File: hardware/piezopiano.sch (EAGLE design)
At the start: 87 parts, among them J1 CON2, Q1 DMN3404L, Q2 DMN3404L, Q3 DMN3404L, Q4 DMN3404L, Q5 DMN3404L, Q6 DMN3404L, Q7 DMN3404L, Q8 DMN3404L, U1 ATMEGA4809, U2 CH340E_MSOP10

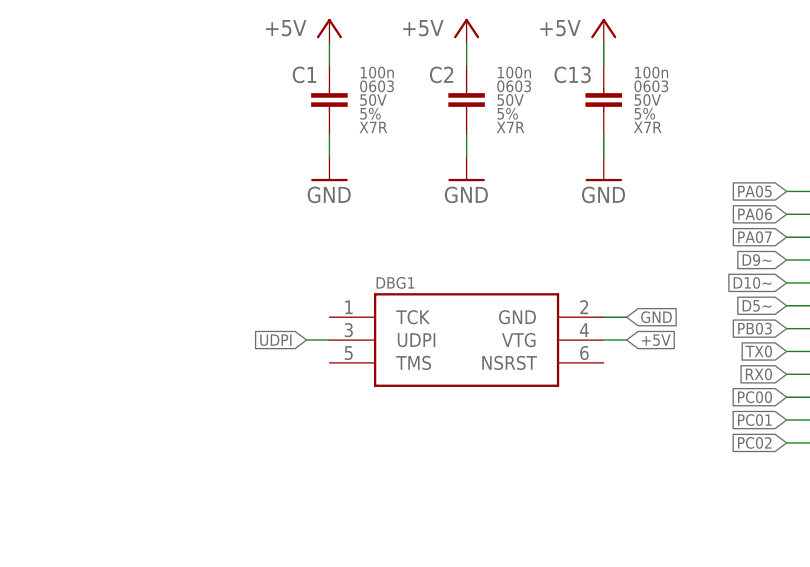
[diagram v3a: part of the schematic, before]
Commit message: Added PCB artwork
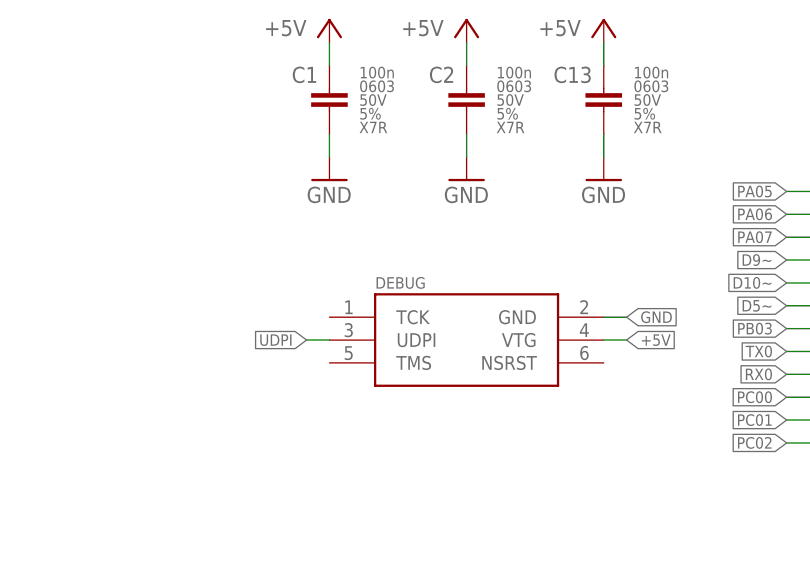
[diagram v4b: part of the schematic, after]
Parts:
- renumbered DBG1 to DEBUG
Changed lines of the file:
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@@
 <part name="R22" library="zaan-Resistors" library_urn="urn:adsk.eagle:library:16759442" deviceset="1KOHM" device="-0603-1/10W-1%" package3d_urn="urn:adsk.eagle:package:16759452/3" value="1k"/>
 <part name="U1" library="zaan-IC-Microcontroller" library_urn="urn:adsk.eagle:library:16759236" deviceset="ATMEGA4809" device="" package3d_urn="urn:adsk.eagle:package:30825331/1" value="ATMEGA4809"/>
-<part name="DBG1" library="zaan-Connectors" library_urn="urn:adsk.eagle:library:16759010" deviceset="AVR-UPDI-6" device="-SKEDD" package3d_urn="urn:adsk.eagle:package:16760574/1"/>
+<part name="DEBUG" library="zaan-Connectors" library_urn="urn:adsk.eagle:library:16759010" deviceset="AVR-UPDI-6" device="-SKEDD" package3d_urn="urn:adsk.eagle:package:16760574/1"/>
 <part name="C13" library="zaan-Capacitors" library_urn="urn:adsk.eagle:library:16758934" deviceset="100NF" device="-0603-50V-5%" package3d_urn="urn:adsk.eagle:package:16758953/4" value="100n"/>
 <part name="GND42" library="supply1" library_urn="urn:adsk.eagle:library:371" deviceset="GND" device=""/>
@@
 <part name="C11" library="zaan-Capacitors" library_urn="urn:adsk.eagle:library:16758934" deviceset="100NF" device="-0603-50V-5%" package3d_urn="urn:adsk.eagle:package:16758953/4" value="100n"/>
 <part name="GND37" library="supply1" library_urn="urn:adsk.eagle:library:371" deviceset="GND" device=""/>
-<part name="JP1" library="zaan-No-Category" library_urn="urn:adsk.eagle:library:16759360" deviceset="PINROW-1X5" device="" package3d_urn="urn:adsk.eagle:package:31104797/4"/>
-<part name="JP2" library="zaan-No-Category" library_urn="urn:adsk.eagle:library:16759360" deviceset="PINROW-1X5" device="" package3d_urn="urn:adsk.eagle:package:31104797/4"/>
-<part name="JP3" library="zaan-No-Category" library_urn="urn:adsk.eagle:library:16759360" deviceset="PINROW-1X5" device="" package3d_urn="urn:adsk.eagle:package:31104797/4"/>
-<part name="JP4" library="zaan-No-Category" library_urn="urn:adsk.eagle:library:16759360" deviceset="PINROW-1X5" device="" package3d_urn="urn:adsk.eagle:package:31104797/4"/>
-<part name="JP5" library="zaan-No-Category" library_urn="urn:adsk.eagle:library:16759360" deviceset="PINROW-1X5" device="" package3d_urn="urn:adsk.eagle:package:31104797/4"/>
+<part name="JP1" library="zaan-No-Category" library_urn="urn:adsk.eagle:library:16759360" deviceset="PINROW-1X5" device="" package3d_urn="urn:adsk.eagle:package:31104797/6"/>
+<part name="JP2" library="zaan-No-Category" library_urn="urn:adsk.eagle:library:16759360" deviceset="PINROW-1X5" device="" package3d_urn="urn:adsk.eagle:package:31104797/6"/>
+<part name="JP3" library="zaan-No-Category" library_urn="urn:adsk.eagle:library:16759360" deviceset="PINROW-1X5" device="" package3d_urn="urn:adsk.eagle:package:31104797/6"/>
+<part name="JP4" library="zaan-No-Category" library_urn="urn:adsk.eagle:library:16759360" deviceset="PINROW-1X5" device="" package3d_urn="urn:adsk.eagle:package:31104797/6"/>
+<part name="JP5" library="zaan-No-Category" library_urn="urn:adsk.eagle:library:16759360" deviceset="PINROW-1X5" device="" package3d_urn="urn:adsk.eagle:package:31104797/6"/>
 <part name="C12" library="zaan-Capacitors" library_urn="urn:adsk.eagle:library:16758934" deviceset="100NF" device="-0603-50V-5%" package3d_urn="urn:adsk.eagle:package:16758953/4" value="100n"/>
 <part name="GND26" library="supply1" library_urn="urn:adsk.eagle:library:371" deviceset="GND" device=""/>
@@
 <part name="D9" library="zaan-Optoelectronics" library_urn="urn:adsk.eagle:library:16759395" deviceset="CHIP-FLAT-Y" device="_0603-0.55MM" package3d_urn="urn:adsk.eagle:package:31105136/2" value="LED_YELLOW"/>
 <part name="D10" library="zaan-Optoelectronics" library_urn="urn:adsk.eagle:library:16759395" deviceset="CHIP-FLAT-Y" device="_0603-0.55MM" package3d_urn="urn:adsk.eagle:package:31105136/2" value="LED_YELLOW"/>
-<part name="JP6" library="zaan-No-Category" library_urn="urn:adsk.eagle:library:16759360" deviceset="PINROW-1X5" device="" package3d_urn="urn:adsk.eagle:package:31104797/4"/>
+<part name="JP6" library="zaan-No-Category" library_urn="urn:adsk.eagle:library:16759360" deviceset="PINROW-1X5" device="" package3d_urn="urn:adsk.eagle:package:31104797/6"/>
 <part name="D11" library="zaan-Optoelectronics" library_urn="urn:adsk.eagle:library:16759395" deviceset="WS2812B" device="" package3d_urn="urn:adsk.eagle:package:31106145/1"/>
 <part name="P+16" library="supply1" library_urn="urn:adsk.eagle:library:371" deviceset="+5V" device=""/>
@@
 <attribute name="VALUE" x="124.46" y="236.22" size="1.778" layer="96"/>
 </instance>
-<instance part="DBG1" gate="G$1" x="33.02" y="208.28" smashed="yes">
+<instance part="DEBUG" gate="G$1" x="33.02" y="208.28" smashed="yes">
 <attribute name="NAME" x="22.86" y="214.63" size="1.27" layer="95" align="center-left"/>
 </instance>
@@
 </segment>
 <segment>
-<pinref part="DBG1" gate="G$1" pin="GND"/>
+<pinref part="DEBUG" gate="G$1" pin="GND"/>
 <wire x1="48.26" y1="210.82" x2="50.8" y2="210.82" width="0.1524" layer="91"/>
 <label x="50.8" y="210.82" size="1.27" layer="95" xref="yes"/>
@@
 </segment>
 <segment>
-<pinref part="DBG1" gate="G$1" pin="VTG"/>
+<pinref part="DEBUG" gate="G$1" pin="VTG"/>
 <wire x1="48.26" y1="208.28" x2="50.8" y2="208.28" width="0.1524" layer="91"/>
 <label x="50.8" y="208.28" size="1.27" layer="95" xref="yes"/>
@@
 <net name="UDPI" class="0">
 <segment>
-<pinref part="DBG1" gate="G$1" pin="UDPI"/>
+<pinref part="DEBUG" gate="G$1" pin="UDPI"/>
 <wire x1="17.78" y1="208.28" x2="15.24" y2="208.28" width="0.1524" layer="91"/>
 <label x="15.24" y="208.28" size="1.27" layer="95" rot="R180" xref="yes"/>

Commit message: Added parts for size reference
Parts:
- added Q9: DNP, zaan-Discrete:DMN3404L
- added R20, R24, R25, R26, R27, R28, R29, R30: 1k, zaan-Resistors:1KOHM-0603-1/10W-1%
- added R31: DNP, zaan-Resistors:DNP-0603
- added R32: DNP, zaan-Resistors:DNP-0805
- added R33: DNP, zaan-Resistors:DNP-1206
- added U3: DNP, zaan-IC-Microcontroller:TINY212
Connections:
- removed net D9: C4.1, S2.P, S2.P@1
- removed net EXT_PH_01: JP1.1
- removed net EXT_PH_02: JP2.1
- removed net EXT_PH_03: JP3.1
- removed net EXT_PH_04: JP4.1
- new net N$21: Q1.G
- new net N$22: D2.A, R24.1
- new net N$23: D5.A, R29.1
- new net N$24: D7.A, R30.1
- new net N$25: D6.A, R20.1
- new net N$26: D8.A, R27.1
- new net N$27: D1.A, R28.1
- new net N$33: D10.A, R25.1
- new net N$34: D9.A, R26.1
- net +5V: now also R20.2, R24.2, R25.2, R26.2, R27.2, R28.2, R29.2, R30.2
- net A0: now also JP1.1
- net A1: now also JP2.1
- net A2: now also JP3.1
- net A3: now also JP4.1
- net D4: now also C3.1, S1.P, S1.P@1; no longer Q1.G
- net D8: no longer C3.1, S1.P, S1.P@1
- net N$12: now also D10.C
- net N$14: now also D7.C
- net N$17: now also D9.C
- net N$2: now also D6.C
- net N$3: now also D1.C
- net N$5: now also D5.C
- net N$7: now also D8.C
- net N$9: now also D2.C
- net PC07: now also C4.1, S2.P, S2.P@1
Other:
- moved on the sheet: D1, D10, D2, D5, D6, D7, D8, D9, LS2, LS3, LS5, LS7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

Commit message: Placement changes
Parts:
- removed R33: DNP, zaan-Resistors:DNP-1206
- removed U3: DNP, zaan-IC-Microcontroller:TINY212
- added R34, R35, R36: 1k, zaan-Resistors:1KOHM-0603-1/10W-1%
- added U5: MSP432P401RIZXHR, zaan-IC-Microcontroller:MSP432P401RIZXHR
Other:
- moved on the sheet: C10, C3, C4, C5, C6, C7, C8, C9, D1, D10, D2, D5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

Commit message: Schematic cleanup
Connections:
- new net N$28: D3.R, R35.2
- new net N$35: D3.G, R34.2
- new net N$36: D3.B, R36.2
- new net N$37: R35.1
- new net N$38: R34.1
- new net N$39: R36.1
- net +5V: now also D3.4, J1.2
- net N$1: now also D11.DIN; no longer J1.2
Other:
- note added: "DNP, Size Reference"
- moved on the sheet: C11, C12, C14, C15, D11, D12, D3, D4, F1, J1, J2, J3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
